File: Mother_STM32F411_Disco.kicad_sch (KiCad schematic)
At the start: 29 parts, among them U1 ESP32-DEVKIT-V1

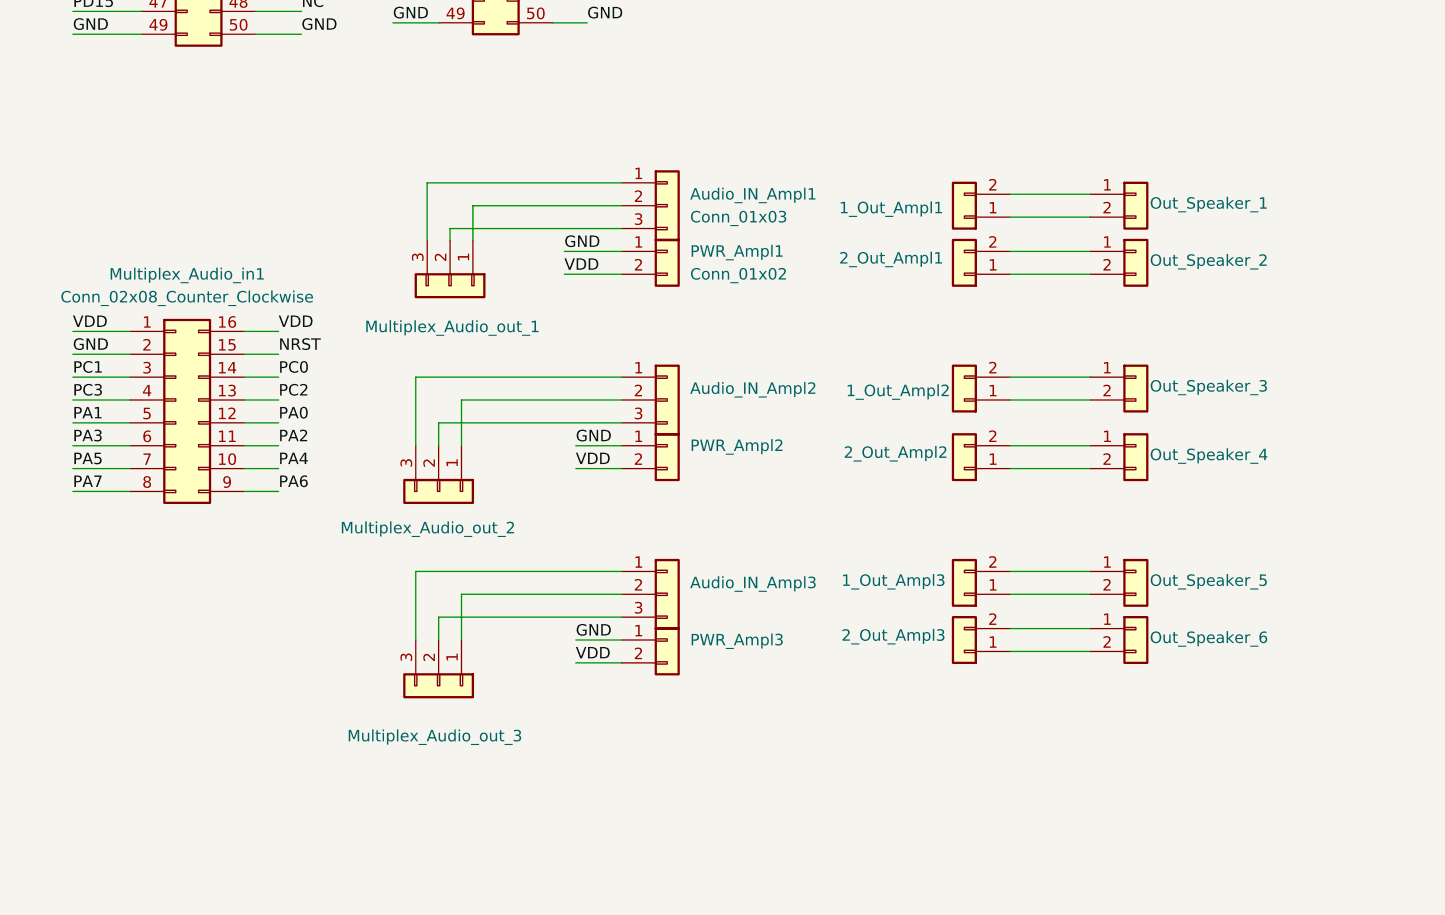
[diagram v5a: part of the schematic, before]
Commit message: Huellas agregadas, src_pwr agregado
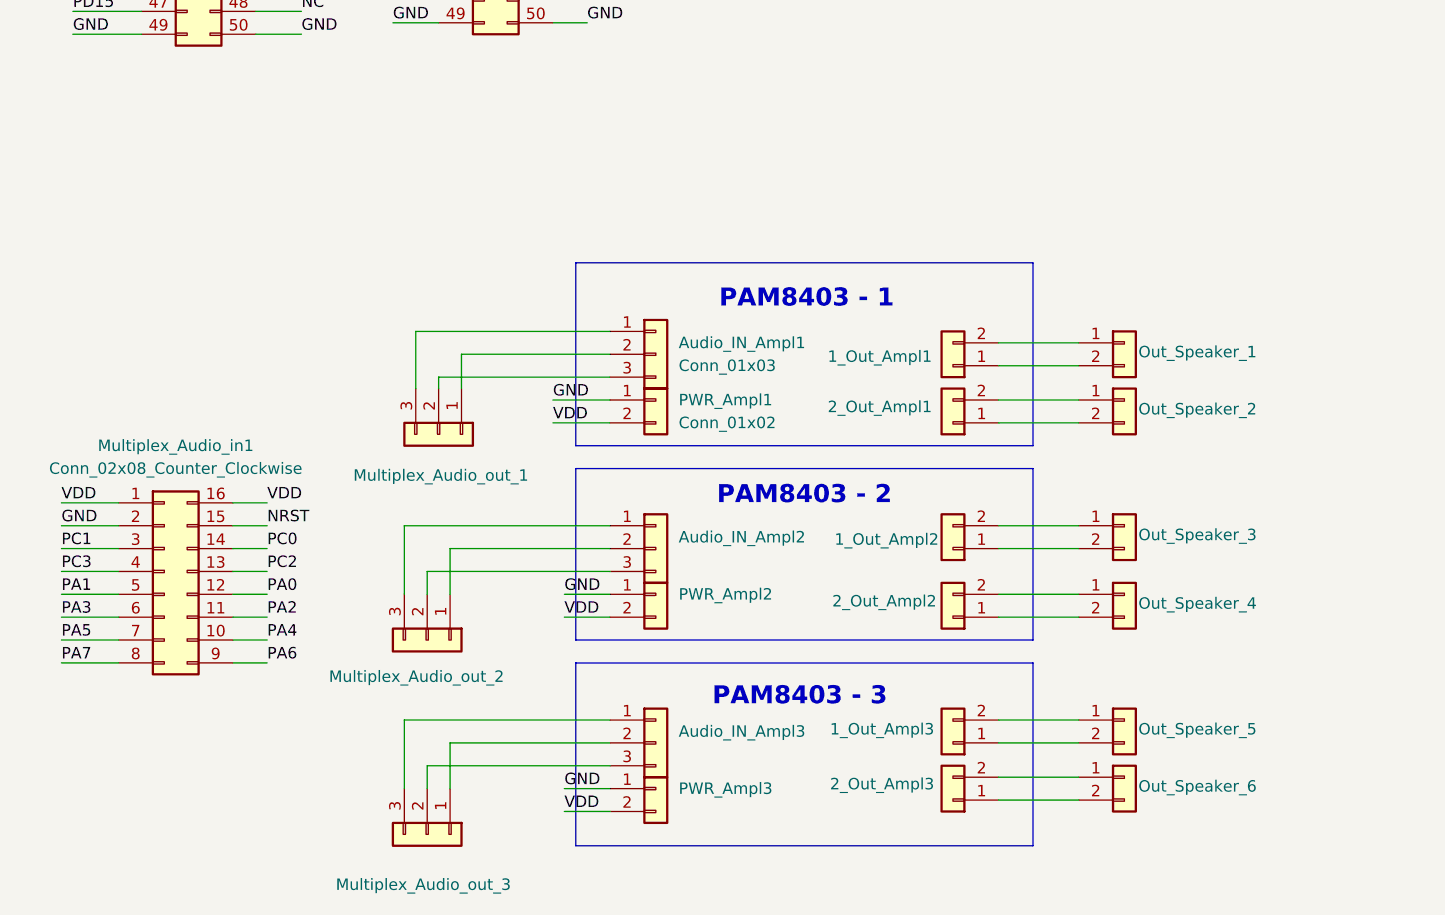
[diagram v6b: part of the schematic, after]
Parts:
- Multiplex_Audio_in1: footprint Connector_PinHeader_1.00mm:PinHeader_2x08_P1.00mm_Vertical -> Connector_PinHeader_2.54mm:PinHeader_2x08_P2.54mm_Vertical
- UART1: footprint Connector_PinSocket_2.54mm:PinSocket_1x04_P2.54mm_Horizontal -> Connector_PinHeader_2.54mm:PinHeader_1x04_P2.54mm_Horizontal
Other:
- note added: "PAM8403 - 1"
- note added: "PAM8403 - 2"
- note added: "PAM8403 - 3"
- moved on the sheet: 1_Out_Ampl1, 1_Out_Ampl2, 1_Out_Ampl3, 2_Out_Ampl1, 2_Out_Ampl2, 2_Out_Ampl3, Audio_IN_Ampl1, Audio_IN_Ampl2, Audio_IN_Ampl3, Multiplex_Audio_in1, Multiplex_Audio_out_1, Multiplex_Audio_out_2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

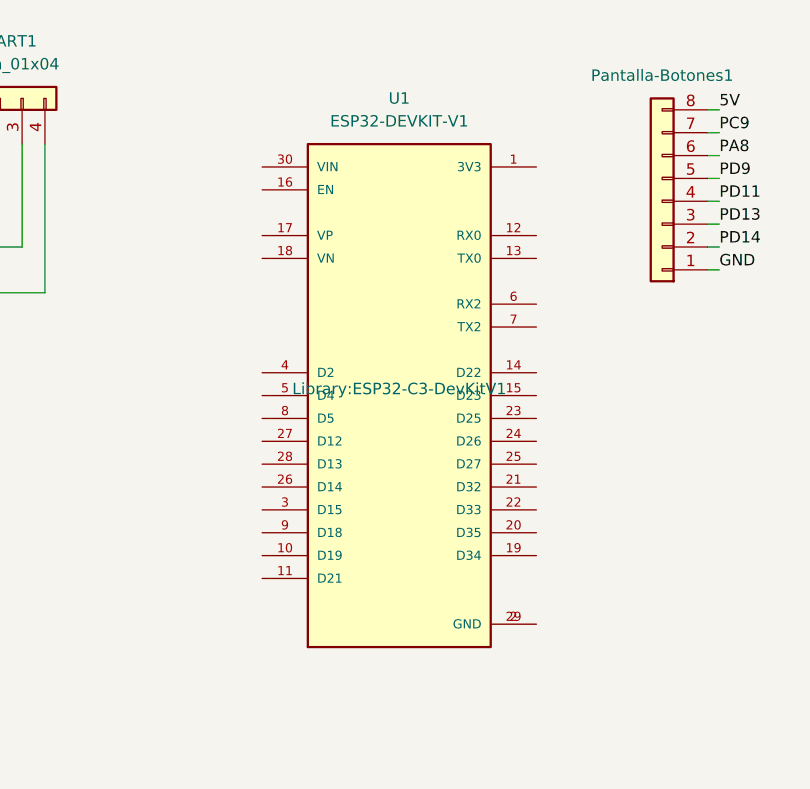
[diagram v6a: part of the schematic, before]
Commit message: SA'18: agregue pistas de la ESP32 y actualice el footprint
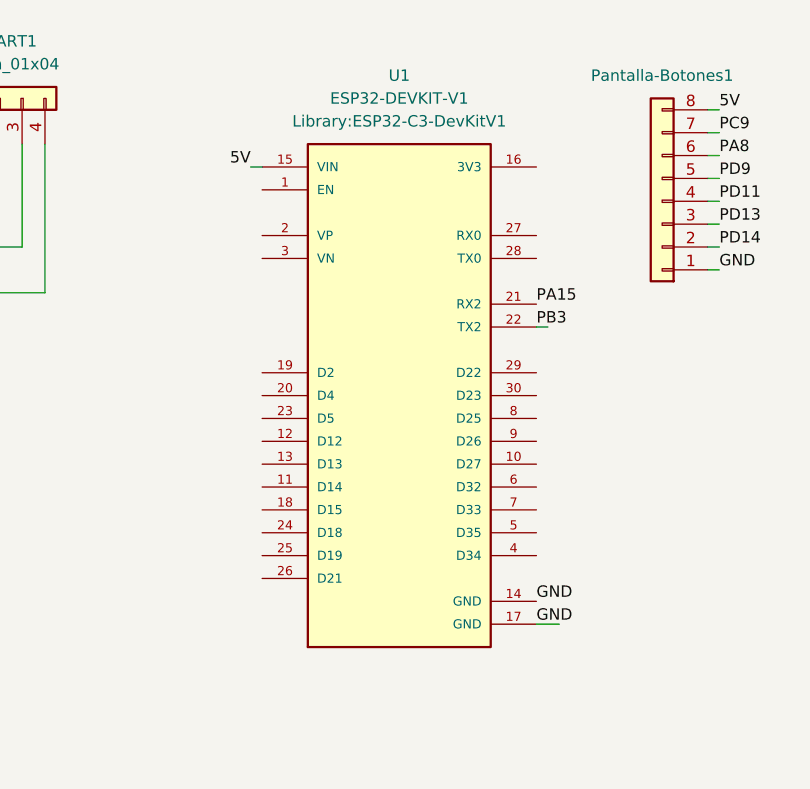
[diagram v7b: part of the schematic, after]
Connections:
- net 5V: now also U1.15 (VIN)
- net GND: now also U1.14 (GND), U1.17 (GND)
- net PA15: now also U1.21 (RX2)
- net PB3: now also U1.22 (TX2)
- net at U1.2 (VP): no longer U1.29 (GND)
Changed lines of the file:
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@@
+	(wire
+		(pts
+			(xy 167.64 59.69) (xy 168.91 59.69)
+		)
+		(stroke
+			(width 0)
+			(type default)
+		)
+	)
 	(wire
 		(pts
@@
 	(wire
 		(pts
+			(xy 170.18 92.71) (xy 167.64 92.71)
+		)
+		(stroke
+			(width 0)
+			(type default)
+		)
+	)
+	(wire
+		(pts
 			(xy 125.73 135.89) (xy 134.62 135.89)
 		)
@@
 		(pts
 			(xy 58.42 64.77) (xy 63.5 64.77)
+		)
+		(stroke
+			(width 0)
+			(type default)
+		)
+	)
+	(wire
+		(pts
+			(xy 135.89 41.91) (xy 137.16 41.91)
 		)
 		(stroke
@@
 		)
 	)
+	(label "5V"
+		(at 135.89 41.91 180)
+		(effects
+			(font
+				(size 1.27 1.27)
+			)
+			(justify right bottom)
+		)
+	)
 	(label "PD9"
 		(at 187.96 43.18 0)
@@
 		)
 	)
+	(label "PA15"
+		(at 167.64 57.15 0)
+		(effects
+			(font
+				(size 1.27 1.27)
+			)
+			(justify left bottom)
+		)
+	)
 	(label "PD14"
 		(at 187.96 50.8 0)
@@
 		)
 	)
+	(label "PB3"
+		(at 167.64 59.69 0)
+		(effects
+			(font
+				(size 1.27 1.27)
+			)
+			(justify left bottom)
+		)
+	)
 	(label "GND"
 		(at 22.86 40.64 0)
@@
 		)
 	)
+	(label "GND"
+		(at 167.64 92.71 0)
+		(effects
+			(font
+				(size 1.27 1.27)
+			)
+			(justify left bottom)
+		)
+	)
 	(label "PE0"
 		(at 58.42 59.69 0)
@@
 	(label "PC3"
 		(at 22.86 50.8 0)
+		(effects
+			(font
+				(size 1.27 1.27)
+			)
+			(justify left bottom)
+		)
+	)
+	(label "GND"
+		(at 167.64 90.17 0)
 		(effects
 			(font
@@
 		(fields_autoplaced yes)
 		(property "Reference" "U1"
+			(at 152.4 31.75 0)
+			(effects
+				(font
+					(size 1.27 1.27)
+				)
+			)
+		)
+		(property "Value" "ESP32-DEVKIT-V1"
 			(at 152.4 34.29 0)
 			(effects
@@
 			)
 		)
-		(property "Value" "ESP32-DEVKIT-V1"
+		(property "Footprint" "Library:ESP32-C3-DevKitV1"
 			(at 152.4 36.83 0)
 			(effects
@@
 					(size 1.27 1.27)
 				)
-			)
-		)
-		(property "Footprint" "Library:ESP32-C3-DevKitV1"
-			(at 152.4 67.31 0)
-			(effects
-				(font
-					(size 1.27 1.27)
-				)
-				(justify bottom)
 			)
 		)
@@
 		(pin "9"
 		)
+		(pin "16"
+		)
+		(pin "1"
+		)
+		(pin "19"
+		)
+		(pin "6"
+		)
+		(pin "18"
+		)
+		(pin "26"
+		)
+		(pin "20"
+		)
+		(pin "4"
+		)
+		(pin "5"
+		)
+		(pin "8"
+		)
+		(pin "27"
+		)
+		(pin "28"
+		)
+		(pin "3"
+		)
+		(pin "10"
+		)
+		(pin "14"
+		)
+		(pin "12"
+		)
+		(pin "17"
+		)
+		(pin "24"
+		)
 		(pin "11"
 		)
-		(pin "1"
-		)
-		(pin "26"
-		)
-		(pin "18"
+		(pin "21"
+		)
+		(pin "25"
+		)
+		(pin "23"
 		)
 		(pin "30"
 		)
-		(pin "17"
-		)
-		(pin "16"
-		)
-		(pin "4"
-		)
-		(pin "5"
-		)
-		(pin "8"
-		)
-		(pin "27"
-		)
-		(pin "28"
-		)
-		(pin "3"
-		)
-		(pin "10"
-		)
-		(pin "14"
-		)
-		(pin "12"
-		)
-		(pin "6"
-		)
-		(pin "24"
+		(pin "13"
+		)
+		(pin "22"
 		)
 		(pin "2"
 		)
-		(pin "21"
-		)
-		(pin "25"
-		)
-		(pin "23"
-		)
-		(pin "19"
-		)
-		(pin "13"
-		)
-		(pin "22"
-		)
-		(pin "20"
-		)
 		(pin "7"
